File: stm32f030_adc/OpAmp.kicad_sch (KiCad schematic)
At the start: 16 parts, among them U5 TL072

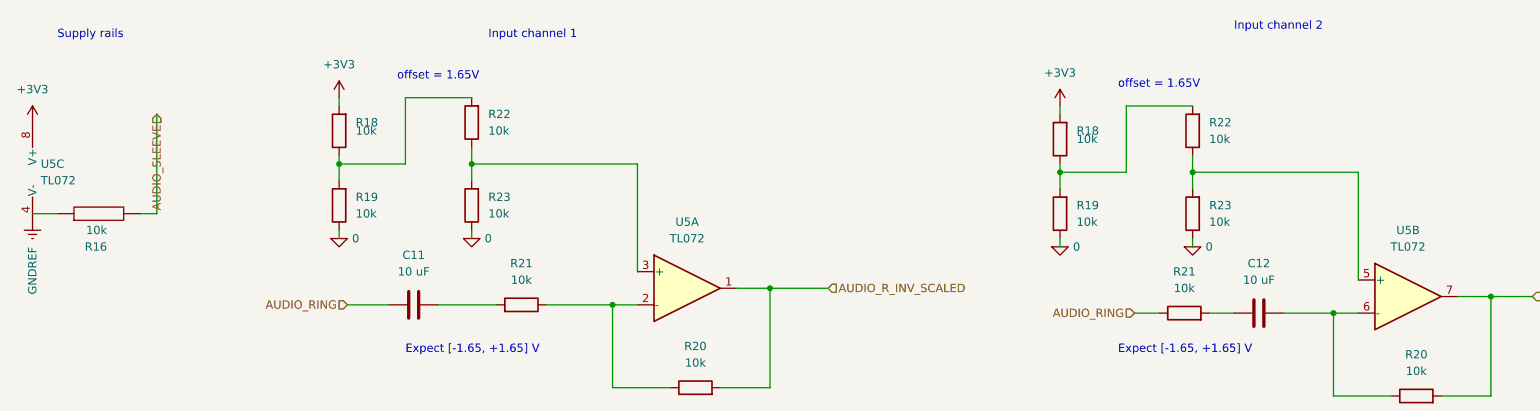
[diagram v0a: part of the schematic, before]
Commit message: [stm32f030_adc] Bug | USB D+ pull-ups, filtering caps for AMS-1117, external 8MHz oscillator
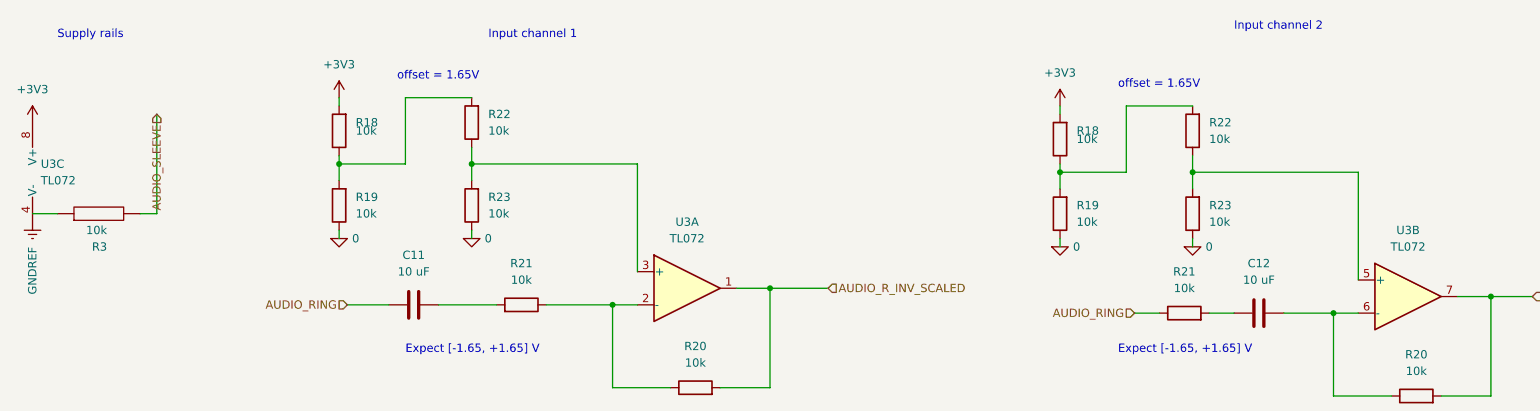
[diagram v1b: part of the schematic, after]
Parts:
- renumbered R16 to R3, U5 to U3

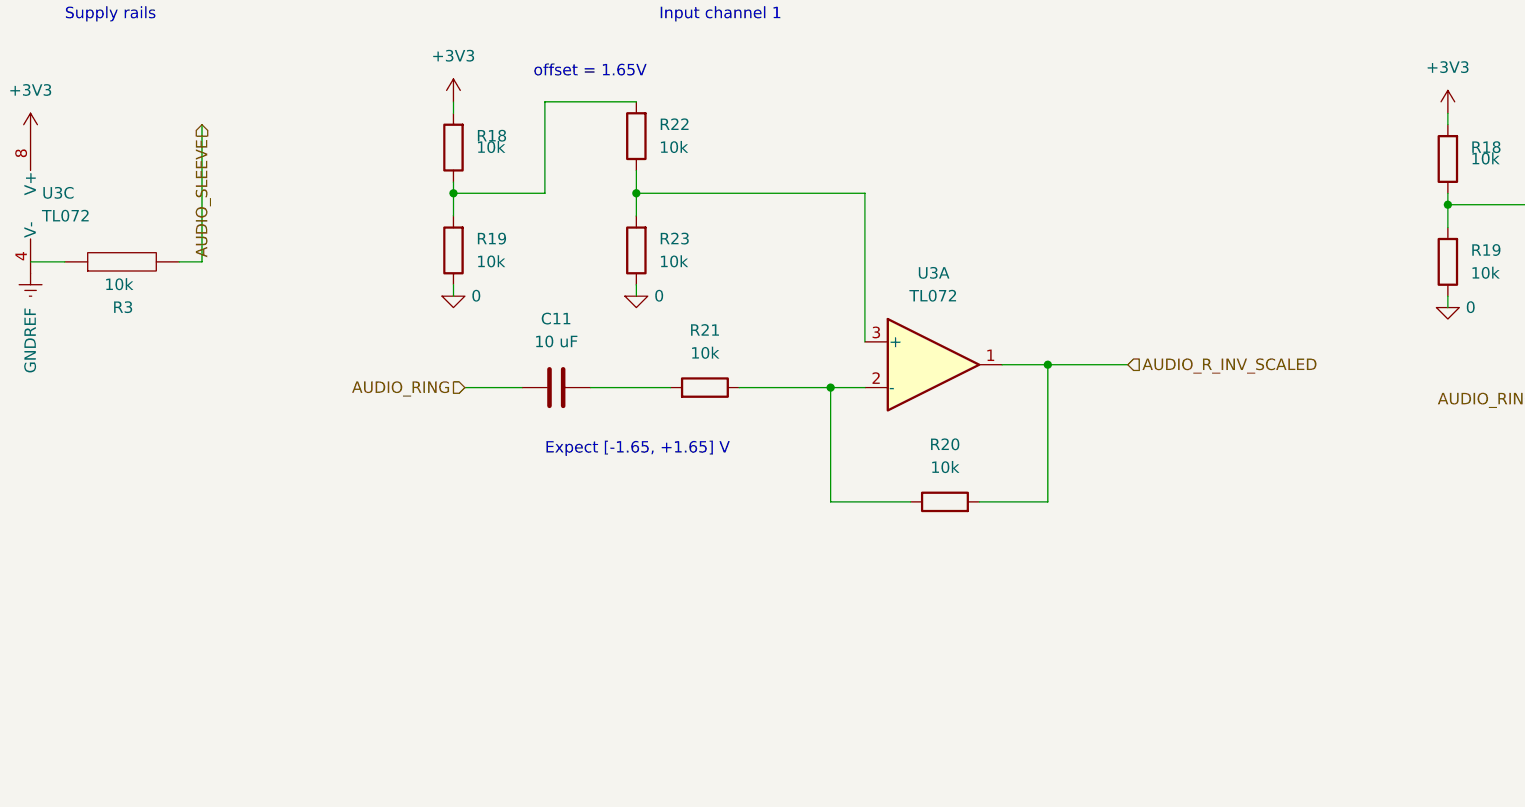
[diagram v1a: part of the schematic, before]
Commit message: [schematics] Impl | Replaced OpAmp w/ BJT-based amplifier (not biased yet), reorganized sheets: separated MCU from gain, added hierarchical connections
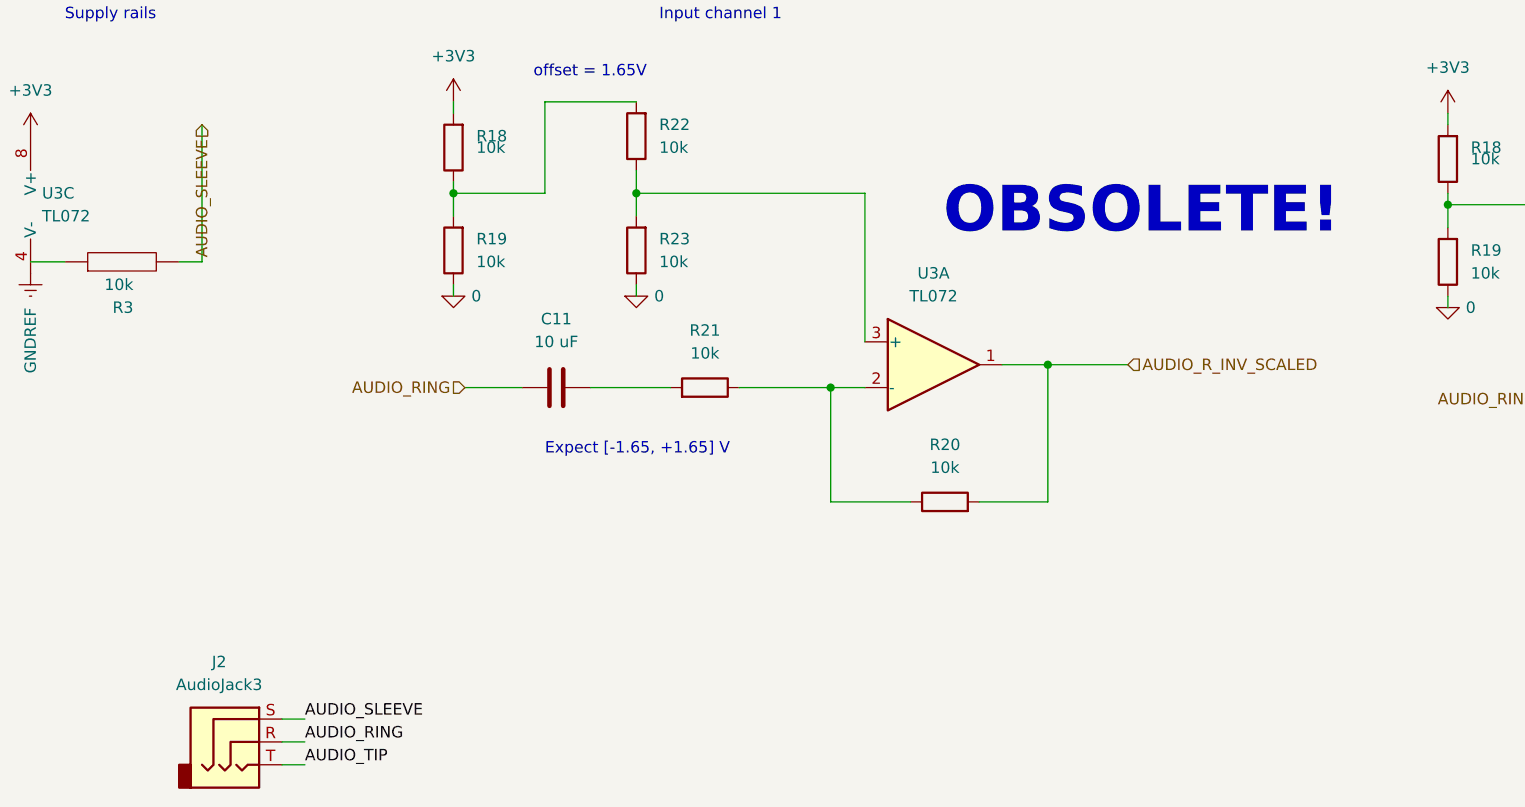
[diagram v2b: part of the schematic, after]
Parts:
- added J2: AudioJack3, symbol Connector:AudioJack3
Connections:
- net AUDIO_RING: now also J2.R
- net AUDIO_SLEEVE: now also J2.S
- new net AUDIO_TIP: J2.T
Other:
- note added: "OBSOLETE!"
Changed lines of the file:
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@@
+	(wire
+		(pts
+			(xy 53.34 147.32) (xy 55.88 147.32)
+		)
+		(stroke
+			(width 0)
+			(type default)
+		)
+	)
 	(wire
 		(pts
@@
 	(wire
 		(pts
+			(xy 53.34 152.4) (xy 55.88 152.4)
+		)
+		(stroke
+			(width 0)
+			(type default)
+		)
+	)
+	(wire
+		(pts
 			(xy 44.45 81.28) (xy 44.45 96.52)
 		)
@@
 		(pts
 			(xy 92.71 88.9) (xy 118.11 88.9)
+		)
+		(stroke
+			(width 0)
+			(type default)
+		)
+	)
+	(wire
+		(pts
+			(xy 53.34 149.86) (xy 55.88 149.86)
 		)
 		(stroke
@@
 		)
 	)
+	(text "OBSOLETE!\n"
+		(exclude_from_sim no)
+		(at 148.844 90.932 0)
+		(effects
+			(font
+				(size 5.08 5.08)
+				(thickness 1.016)
+				(bold yes)
+				(color 255 2 0 1)
+			)
+		)
+	)
 	(text "Expect [-1.65, +1.65] V"
 		(exclude_from_sim no)
@@
 		(exclude_from_sim no)
 		(at 209.55 68.58 0)
+		(effects
+			(font
+				(size 1.27 1.27)
+			)
+			(justify left bottom)
+		)
+	)
+	(label "AUDIO_SLEEVE"
+		(at 55.88 147.32 0)
+		(fields_autoplaced yes)
+		(effects
+			(font
+				(size 1.27 1.27)
+			)
+			(justify left bottom)
+		)
+	)
+	(label "AUDIO_RING"
+		(at 55.88 149.86 0)
+		(fields_autoplaced yes)
+		(effects
+			(font
+				(size 1.27 1.27)
+			)
+			(justify left bottom)
+		)
+	)
+	(label "AUDIO_TIP"
+		(at 55.88 152.4 0)
+		(fields_autoplaced yes)
 		(effects
 			(font
@@
 					(unit 1)
 				)
+			)
+		)
+	)
+	(symbol
+		(lib_id "Connector:AudioJack3")
+		(at 48.26 149.86 0)
+		(unit 1)
+		(exclude_from_sim no)
+		(in_bom yes)
+		(on_board yes)
+		(dnp no)
+		(fields_autoplaced yes)
+		(property "Reference" "J2"
+			(at 46.355 140.97 0)
+			(effects
+				(font
+					(size 1.27 1.27)
+				)
+			)
+		)
+		(property "Value" "AudioJack3"
+			(at 46.355 143.51 0)
+			(effects
+				(font
+					(size 1.27 1.27)
+				)
+			)
+		)
+		(property "Footprint" ""
+			(at 48.26 149.86 0)
+			(effects
+				(font
+					(size 1.27 1.27)
+				)
+				(hide yes)
+			)
+		)
+		(property "Datasheet" "~"
+			(at 48.26 149.86 0)
+			(effects
+				(font
+					(size 1.27 1.27)
+				)
+				(hide yes)
+			)
+		)
+		(property "Description" ""
+			(at 48.26 149.86 0)
+			(effects
+				(font
+					(size 1.27 1.27)
+				)
+				(hide yes)
+			)
+		)
+		(pin "R"
+		)
+		(pin "S"
+		)
+		(pin "T"
+		)
+		(instances
+			(project "stm32f030_adc"
+				(path "/85629656-c73b-4e1f-b8e8-4366f4b01266/b4185304-bcce-4cb1-98f3-8bffc8e76c1e"
+					(reference "J2")
+					(unit 1)
+				)
